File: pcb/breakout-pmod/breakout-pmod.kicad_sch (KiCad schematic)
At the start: 13 parts, among them J1 FX18-120P-0.8SV20

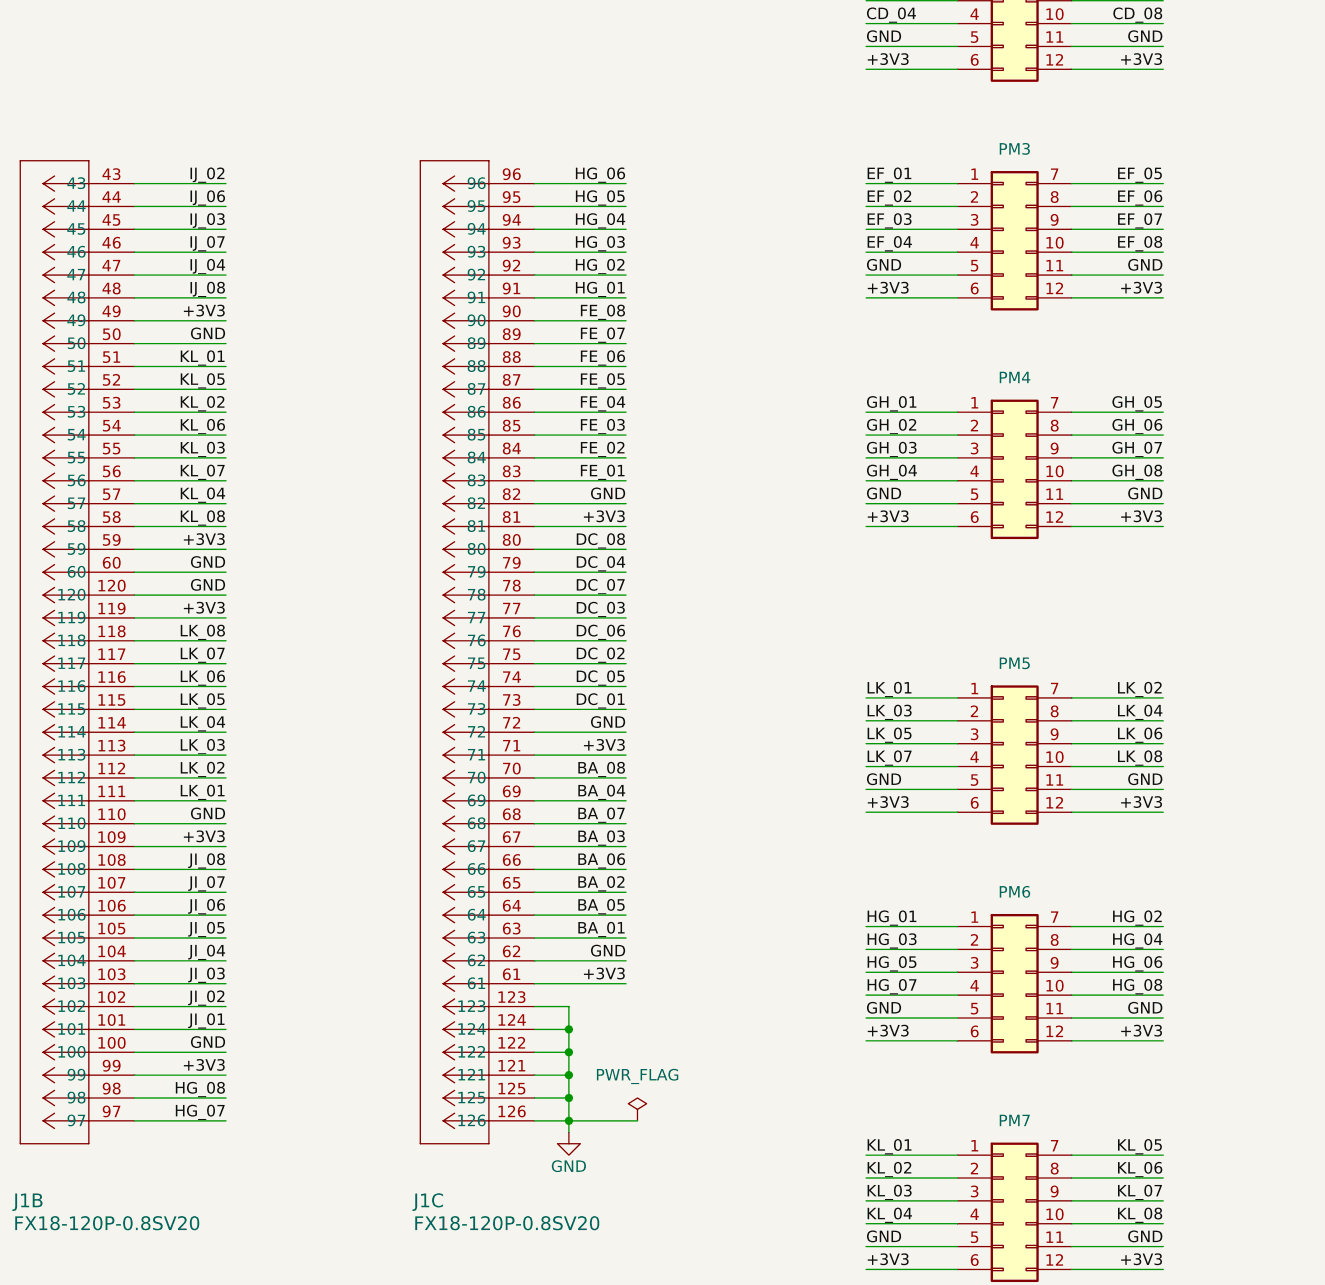
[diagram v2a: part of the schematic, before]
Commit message: [pmod] fix order of HG pmod
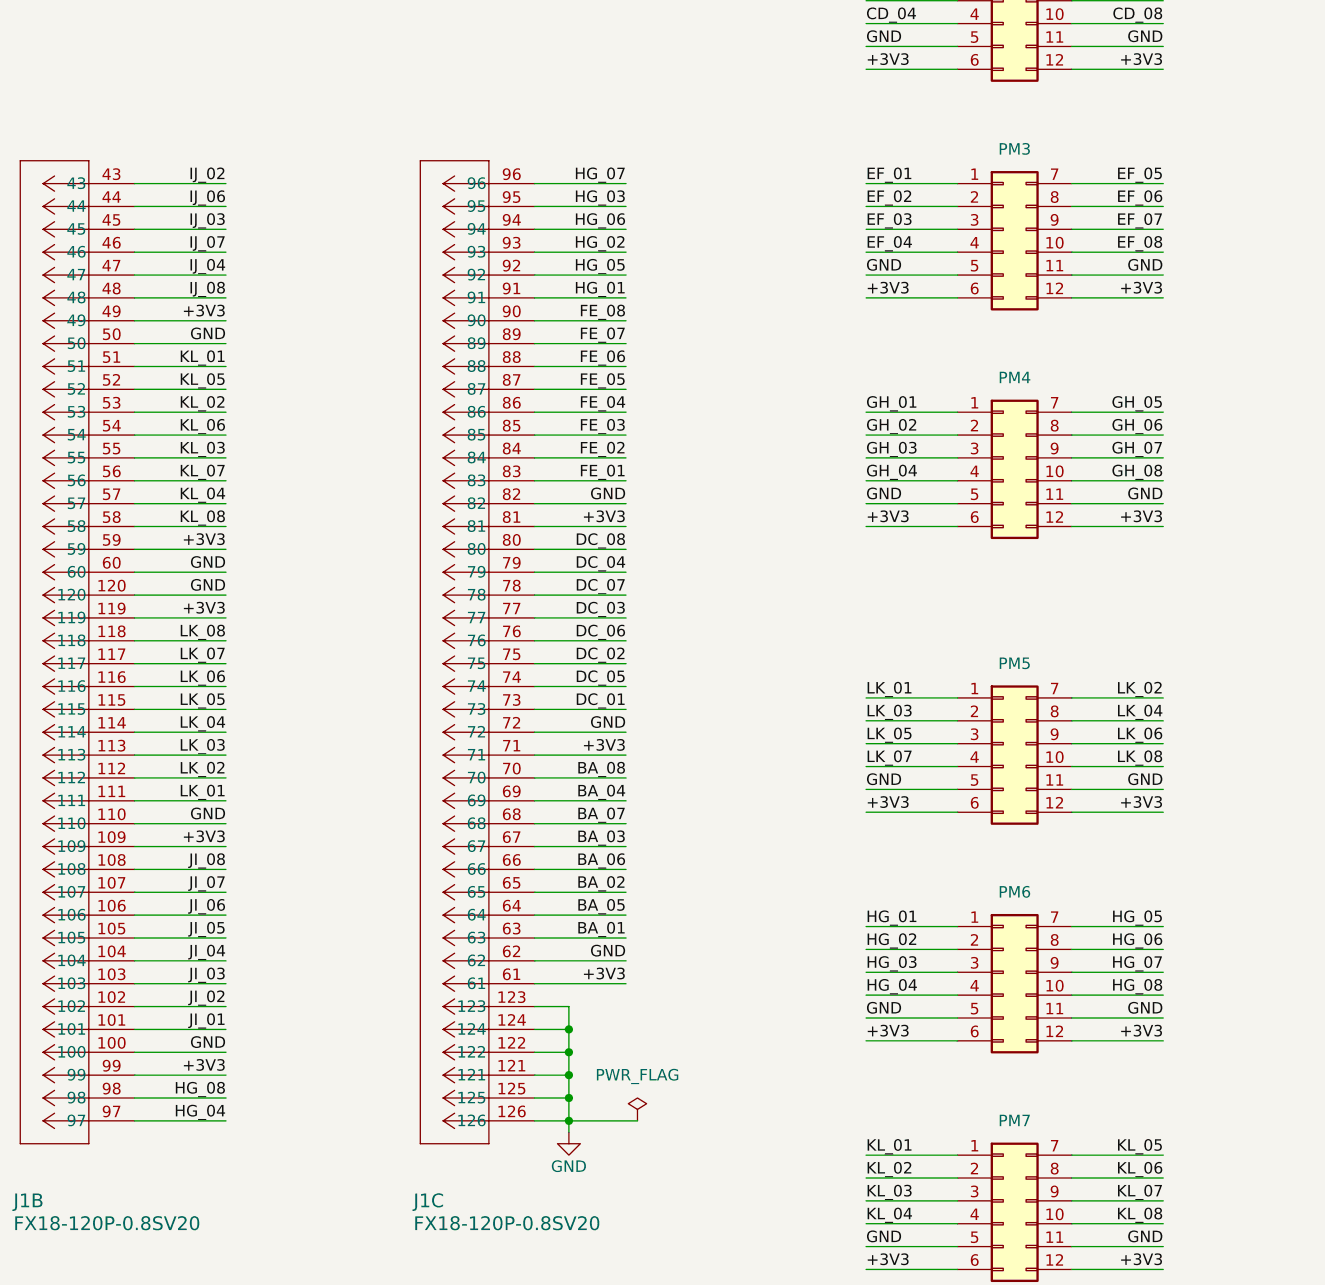
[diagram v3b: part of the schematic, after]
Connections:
- net HG_02: now also J1.93, PM6.2 (Pin_2); no longer J1.92, PM6.7 (Pin_7)
- net HG_03: now also J1.95, PM6.3 (Pin_3); no longer J1.93, PM6.2 (Pin_2)
- net HG_04: now also J1.97, PM6.4 (Pin_4); no longer J1.94, PM6.8 (Pin_8)
- net HG_05: now also J1.92, PM6.7 (Pin_7); no longer J1.95, PM6.3 (Pin_3)
- net HG_06: now also J1.94, PM6.8 (Pin_8); no longer J1.96, PM6.9 (Pin_9)
- net HG_07: now also J1.96, PM6.9 (Pin_9); no longer J1.97, PM6.4 (Pin_4)
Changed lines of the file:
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@@
 	)
 	(label "HG_03"
-		(at 165.1 175.26 0)
+		(at 165.1 177.8 0)
 		(fields_autoplaced yes)
 		(effects
@@
 	)
 	(label "HG_04"
-		(at 198.12 175.26 180)
-		(fields_autoplaced yes)
-		(effects
-			(font
-				(size 1.27 1.27)
-			)
-			(justify right bottom)
+		(at 165.1 180.34 0)
+		(fields_autoplaced yes)
+		(effects
+			(font
+				(size 1.27 1.27)
+			)
+			(justify left bottom)
 		)
 	)
@@
 	)
 	(label "HG_06"
-		(at 138.43 90.17 180)
+		(at 138.43 95.25 180)
 		(fields_autoplaced yes)
 		(effects
@@
 	)
 	(label "HG_02"
-		(at 198.12 172.72 180)
-		(fields_autoplaced yes)
-		(effects
-			(font
-				(size 1.27 1.27)
-			)
-			(justify right bottom)
+		(at 165.1 175.26 0)
+		(fields_autoplaced yes)
+		(effects
+			(font
+				(size 1.27 1.27)
+			)
+			(justify left bottom)
 		)
 	)
@@
 	)
 	(label "HG_04"
-		(at 138.43 95.25 180)
+		(at 93.98 194.31 180)
 		(fields_autoplaced yes)
 		(effects
@@
 	)
 	(label "HG_05"
-		(at 138.43 92.71 180)
+		(at 138.43 100.33 180)
 		(fields_autoplaced yes)
 		(effects
@@
 	)
 	(label "HG_06"
-		(at 198.12 177.8 180)
+		(at 198.12 175.26 180)
 		(fields_autoplaced yes)
 		(effects
@@
 	)
 	(label "HG_07"
-		(at 93.98 194.31 180)
+		(at 138.43 90.17 180)
 		(fields_autoplaced yes)
 		(effects
@@
 	)
 	(label "HG_02"
-		(at 138.43 100.33 180)
+		(at 138.43 97.79 180)
 		(fields_autoplaced yes)
 		(effects
@@
 	)
 	(label "HG_05"
-		(at 165.1 177.8 0)
-		(fields_autoplaced yes)
-		(effects
-			(font
-				(size 1.27 1.27)
-			)
-			(justify left bottom)
+		(at 198.12 172.72 180)
+		(fields_autoplaced yes)
+		(effects
+			(font
+				(size 1.27 1.27)
+			)
+			(justify right bottom)
 		)
 	)
 	(label "HG_07"
-		(at 165.1 180.34 0)
-		(fields_autoplaced yes)
-		(effects
-			(font
-				(size 1.27 1.27)
-			)
-			(justify left bottom)
+		(at 198.12 177.8 180)
+		(fields_autoplaced yes)
+		(effects
+			(font
+				(size 1.27 1.27)
+			)
+			(justify right bottom)
 		)
 	)
@@
 	)
 	(label "HG_03"
-		(at 138.43 97.79 180)
-		(fields_autoplaced yes)
-		(effects
+		(at 138.43 92.71 180)
+		(fields_autoplaced yes)
+		(effects

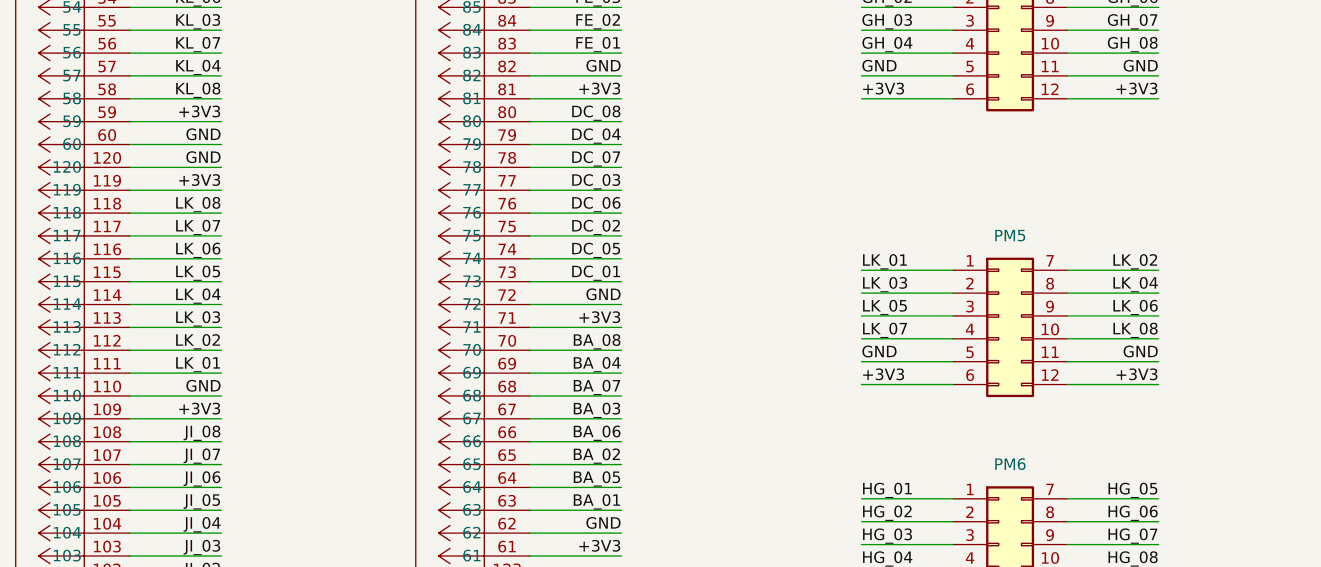
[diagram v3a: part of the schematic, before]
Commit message: [pmod] fix order of LK pmod
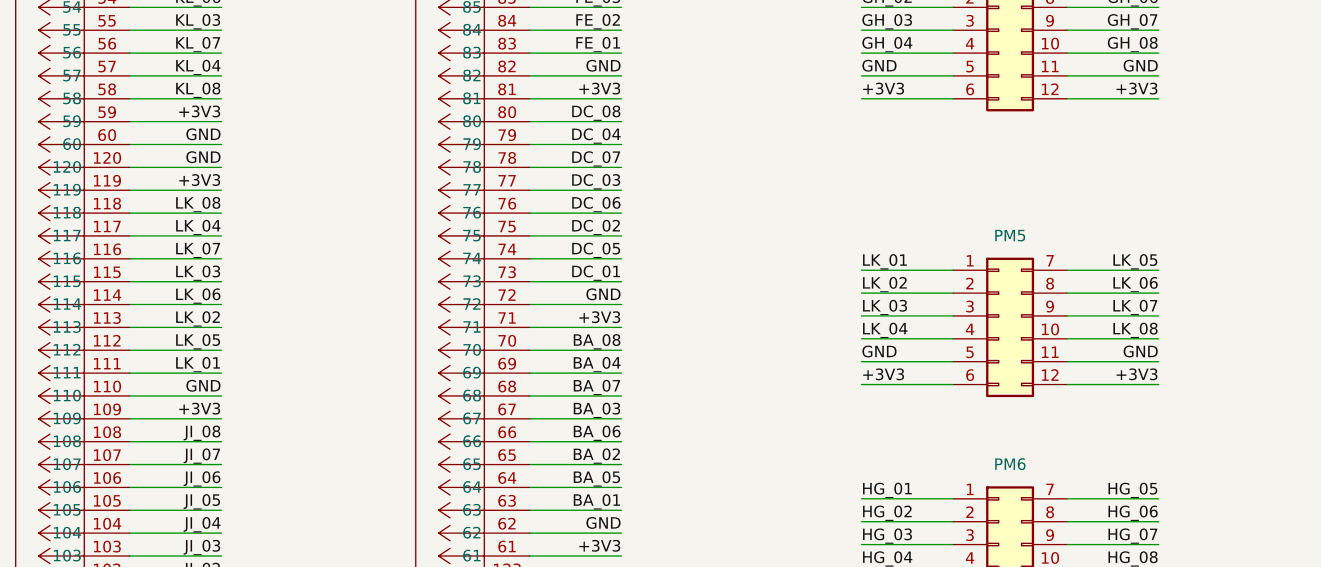
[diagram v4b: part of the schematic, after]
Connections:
- net LK_02: now also J1.113, PM5.2 (Pin_2); no longer J1.112, PM5.7 (Pin_7)
- net LK_03: now also J1.115, PM5.3 (Pin_3); no longer J1.113, PM5.2 (Pin_2)
- net LK_04: now also J1.117, PM5.4 (Pin_4); no longer J1.114, PM5.8 (Pin_8)
- net LK_05: now also J1.112, PM5.7 (Pin_7); no longer J1.115, PM5.3 (Pin_3)
- net LK_06: now also J1.114, PM5.8 (Pin_8); no longer J1.116, PM5.9 (Pin_9)
- net LK_07: now also J1.116, PM5.9 (Pin_9); no longer J1.117, PM5.4 (Pin_4)
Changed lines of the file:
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@@
 	)
 	(label "LK_07"
-		(at 165.1 154.94 0)
-		(fields_autoplaced yes)
-		(effects
-			(font
-				(size 1.27 1.27)
-			)
-			(justify left bottom)
+		(at 198.12 152.4 180)
+		(fields_autoplaced yes)
+		(effects
+			(font
+				(size 1.27 1.27)
+			)
+			(justify right bottom)
 		)
 	)
@@
 	)
 	(label "LK_03"
-		(at 93.98 153.67 180)
+		(at 93.98 148.59 180)
 		(fields_autoplaced yes)
 		(effects
@@
 	)
 	(label "LK_05"
-		(at 165.1 152.4 0)
-		(fields_autoplaced yes)
-		(effects
-			(font
-				(size 1.27 1.27)
-			)
-			(justify left bottom)
+		(at 198.12 147.32 180)
+		(fields_autoplaced yes)
+		(effects
+			(font
+				(size 1.27 1.27)
+			)
+			(justify right bottom)
 		)
 	)
@@
 	)
 	(label "LK_02"
-		(at 198.12 147.32 180)
-		(fields_autoplaced yes)
-		(effects
-			(font
-				(size 1.27 1.27)
-			)
-			(justify right bottom)
+		(at 165.1 149.86 0)
+		(fields_autoplaced yes)
+		(effects
+			(font
+				(size 1.27 1.27)
+			)
+			(justify left bottom)
 		)
 	)
@@
 	)
 	(label "LK_05"
-		(at 93.98 148.59 180)
+		(at 93.98 156.21 180)
 		(fields_autoplaced yes)
 		(effects
@@
 	)
 	(label "LK_07"
-		(at 93.98 143.51 180)
+		(at 93.98 146.05 180)
 		(fields_autoplaced yes)
 		(effects
@@
 	)
 	(label "LK_06"
-		(at 93.98 146.05 180)
+		(at 93.98 151.13 180)
 		(fields_autoplaced yes)
 		(effects
@@
 	)
 	(label "LK_06"
-		(at 198.12 152.4 180)
+		(at 198.12 149.86 180)
 		(fields_autoplaced yes)
 		(effects
@@
 	)
 	(label "LK_04"
-		(at 198.12 149.86 180)
-		(fields_autoplaced yes)
-		(effects
-			(font
-				(size 1.27 1.27)
-			)
-			(justify right bottom)
+		(at 165.1 154.94 0)
+		(fields_autoplaced yes)
+		(effects
+			(font
+				(size 1.27 1.27)
+			)
+			(justify left bottom)
 		)
 	)
@@
 	)
 	(label "LK_02"
-		(at 93.98 156.21 180)
+		(at 93.98 153.67 180)
 		(fields_autoplaced yes)
 		(effects
@@
 	)
 	(label "LK_03"
-		(at 165.1 149.86 0)
+		(at 165.1 152.4 0)
 		(fields_autoplaced yes)
 		(effects
@@
 	)
 	(label "LK_04"
-		(at 93.98 151.13 180)
-		(fields_autoplaced yes)
-		(effects
+		(at 93.98 143.51 180)
+		(fields_autoplaced yes)
+		(effects
